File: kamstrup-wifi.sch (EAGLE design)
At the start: 25 parts, among them T1 BT137, T2 BT137, U1 ESP8266-07, U2 MCP1316T-29LE/OT

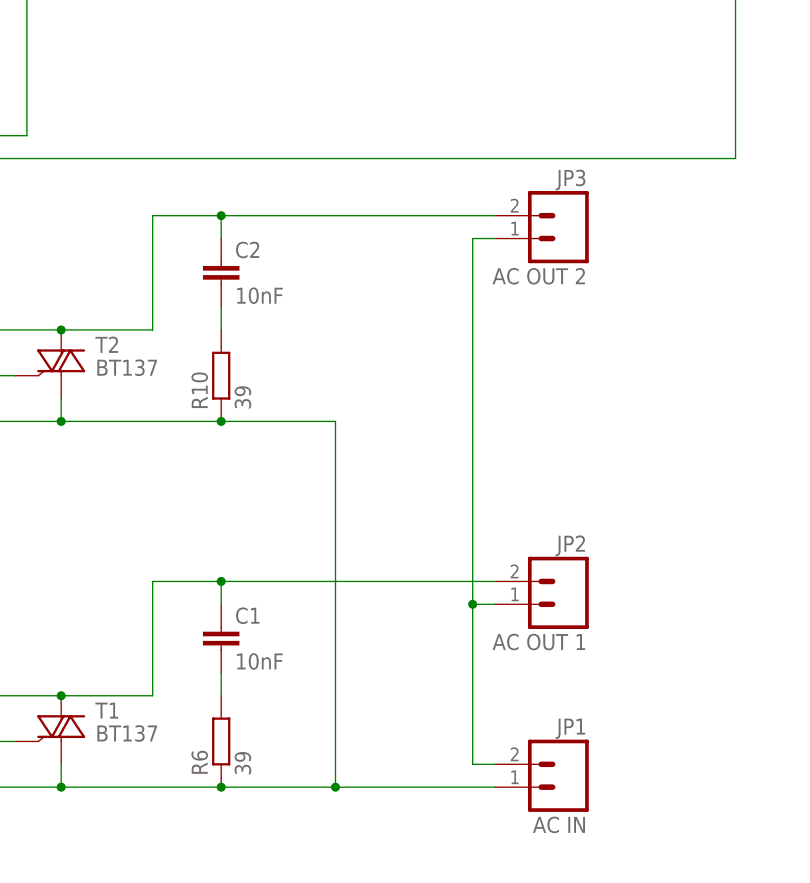
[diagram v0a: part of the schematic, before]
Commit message: rotated jp1, jp3 and jp3
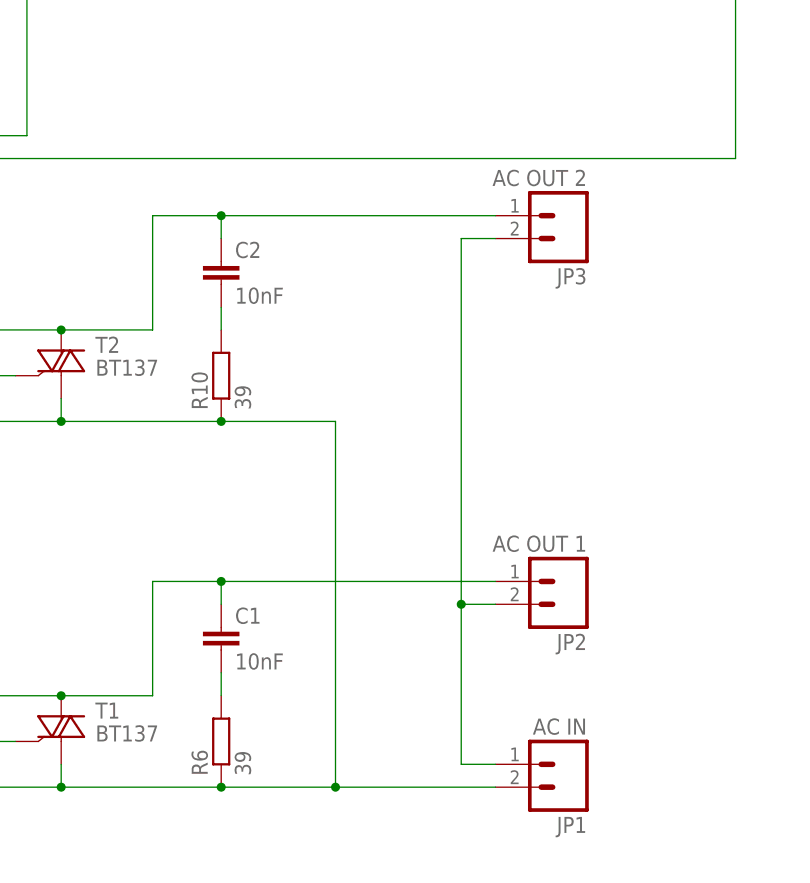
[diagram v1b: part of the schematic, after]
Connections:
- net N$15: now also JP2.1; no longer JP2.2
- net N$18: now also JP1.1, JP2.2, JP3.2; no longer JP1.2, JP2.1, JP3.1
- net N$8: now also JP3.1; no longer JP3.2
- net N$9: now also JP1.2; no longer JP1.1
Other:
- moved on the sheet: JP1, JP2, JP3
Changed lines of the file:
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@@
 <?xml version="1.0" encoding="utf-8"?>
 <!DOCTYPE eagle SYSTEM "eagle.dtd">
-<eagle version="8.2.1">
+<eagle version="8.4.0">
 <drawing>
 <settings>
 <setting alwaysvectorfont="yes"/>
+<setting keepoldvectorfont="yes"/>
 <setting verticaltext="up"/>
 </settings>
@@
 <instance part="R10" gate="G$1" x="97.79" y="-31.75" rot="R90"/>
 <instance part="C2" gate="G$1" x="97.79" y="-19.05"/>
-<instance part="JP3" gate="G$1" x="135.89" y="-16.51" rot="MR0"/>
+<instance part="JP3" gate="G$1" x="135.89" y="-13.97" rot="R180"/>
 <instance part="OK1" gate="-1" x="46.99" y="-72.39"/>
 <instance part="GND2" gate="1" x="31.75" y="-82.55"/>
@@
 <instance part="R6" gate="G$1" x="97.79" y="-72.39" rot="R90"/>
 <instance part="C1" gate="G$1" x="97.79" y="-59.69"/>
-<instance part="JP1" gate="G$1" x="135.89" y="-77.47" rot="MR0"/>
-<instance part="JP2" gate="G$1" x="135.89" y="-57.15" rot="MR0"/>
+<instance part="JP1" gate="G$1" x="135.89" y="-74.93" rot="R180"/>
+<instance part="JP2" gate="G$1" x="135.89" y="-54.61" rot="R180"/>
 <instance part="T1" gate="G$1" x="80.01" y="-72.39"/>
 <instance part="T2" gate="G$1" x="80.01" y="-31.75"/>
@@
 <pinref part="T2" gate="G$1" pin="A2"/>
 <junction x="80.01" y="-26.67"/>
-<pinref part="JP3" gate="G$1" pin="2"/>
+<pinref part="JP3" gate="G$1" pin="1"/>
 <wire x1="128.27" y1="-13.97" x2="97.79" y2="-13.97" width="0.1524" layer="91"/>
 <junction x="97.79" y="-13.97"/>
@@
 <wire x1="110.49" y1="-36.83" x2="110.49" y2="-77.47" width="0.1524" layer="91"/>
 <junction x="97.79" y="-36.83"/>
-<pinref part="JP1" gate="G$1" pin="1"/>
+<pinref part="T2" gate="G$1" pin="A1"/>
+<pinref part="T1" gate="G$1" pin="A1"/>
+<pinref part="JP1" gate="G$1" pin="2"/>
 <wire x1="110.49" y1="-77.47" x2="128.27" y2="-77.47" width="0.1524" layer="91"/>
 <junction x="110.49" y="-77.47"/>
-<pinref part="T2" gate="G$1" pin="A1"/>
-<pinref part="T1" gate="G$1" pin="A1"/>
 </segment>
 </net>
@@
 <pinref part="T1" gate="G$1" pin="A2"/>
 <junction x="80.01" y="-67.31"/>
-<pinref part="JP2" gate="G$1" pin="2"/>
-<wire x1="128.27" y1="-54.61" x2="97.79" y2="-54.61" width="0.1524" layer="91"/>
+<pinref part="JP2" gate="G$1" pin="1"/>
+<wire x1="97.79" y1="-54.61" x2="128.27" y2="-54.61" width="0.1524" layer="91"/>
 <junction x="97.79" y="-54.61"/>
 </segment>
@@
 <pinref part="C1" gate="G$1" pin="2"/>
 <wire x1="97.79" y1="-67.31" x2="97.79" y2="-64.77" width="0.1524" layer="91"/>
-</segment>
-</net>
-<net name="N$18" class="0">
-<segment>
-<wire x1="125.73" y1="-74.93" x2="125.73" y2="-57.15" width="0.1524" layer="91"/>
-<wire x1="125.73" y1="-57.15" x2="125.73" y2="-16.51" width="0.1524" layer="91"/>
-<pinref part="JP1" gate="G$1" pin="2"/>
-<wire x1="128.27" y1="-74.93" x2="125.73" y2="-74.93" width="0.1524" layer="91"/>
-<pinref part="JP2" gate="G$1" pin="1"/>
-<wire x1="128.27" y1="-57.15" x2="125.73" y2="-57.15" width="0.1524" layer="91"/>
-<junction x="125.73" y="-57.15"/>
-<pinref part="JP3" gate="G$1" pin="1"/>
-<wire x1="128.27" y1="-16.51" x2="125.73" y2="-16.51" width="0.1524" layer="91"/>
 </segment>
 </net>
@@
 </segment>
 </net>
+<net name="N$18" class="0">
+<segment>
+<pinref part="JP3" gate="G$1" pin="2"/>
+<wire x1="128.27" y1="-16.51" x2="124.46" y2="-16.51" width="0.1524" layer="91"/>
+<pinref part="JP1" gate="G$1" pin="1"/>
+<wire x1="124.46" y1="-16.51" x2="124.46" y2="-57.15" width="0.1524" layer="91"/>
+<wire x1="124.46" y1="-57.15" x2="124.46" y2="-74.93" width="0.1524" layer="91"/>
+<wire x1="124.46" y1="-74.93" x2="128.27" y2="-74.93" width="0.1524" layer="91"/>
+<pinref part="JP2" gate="G$1" pin="2"/>
+<wire x1="128.27" y1="-57.15" x2="124.46" y2="-57.15" width="0.1524" layer="91"/>
+<junction x="124.46" y="-57.15"/>
+</segment>
+</net>

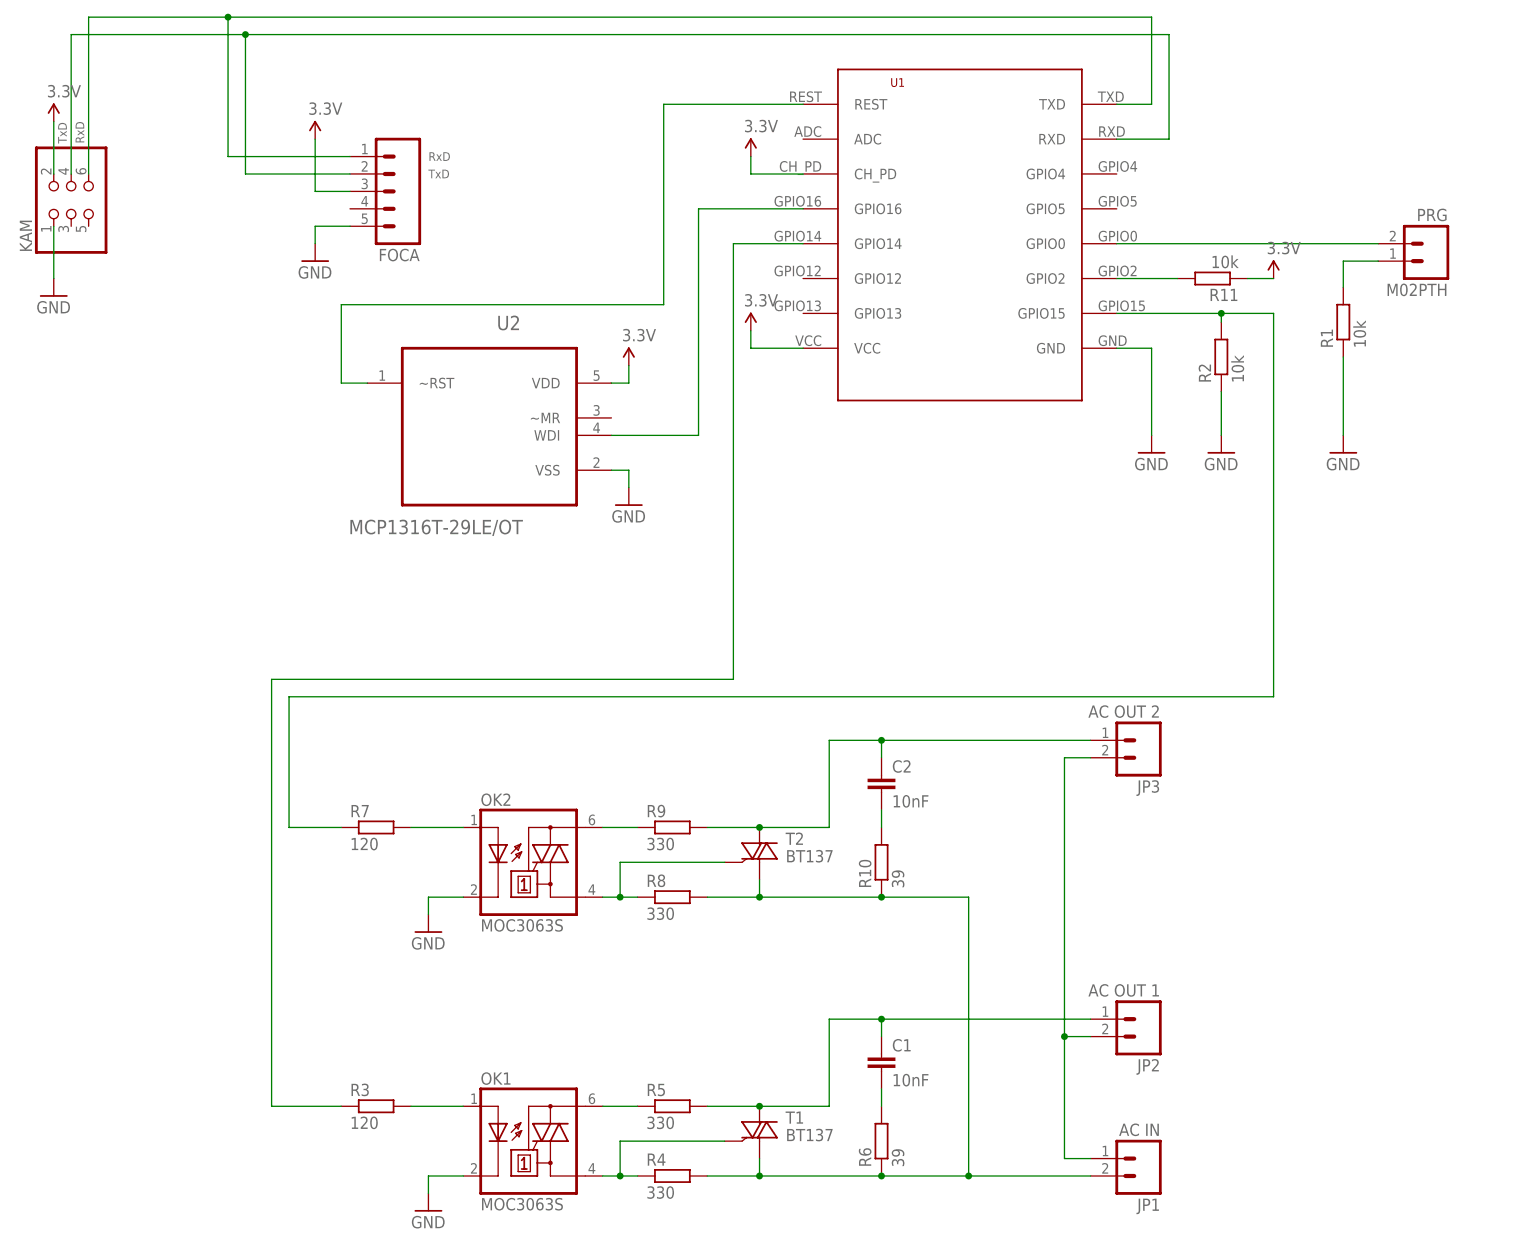
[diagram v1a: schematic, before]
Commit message: removed snubber circuits and external watchdog timer ic now version 1.3.0
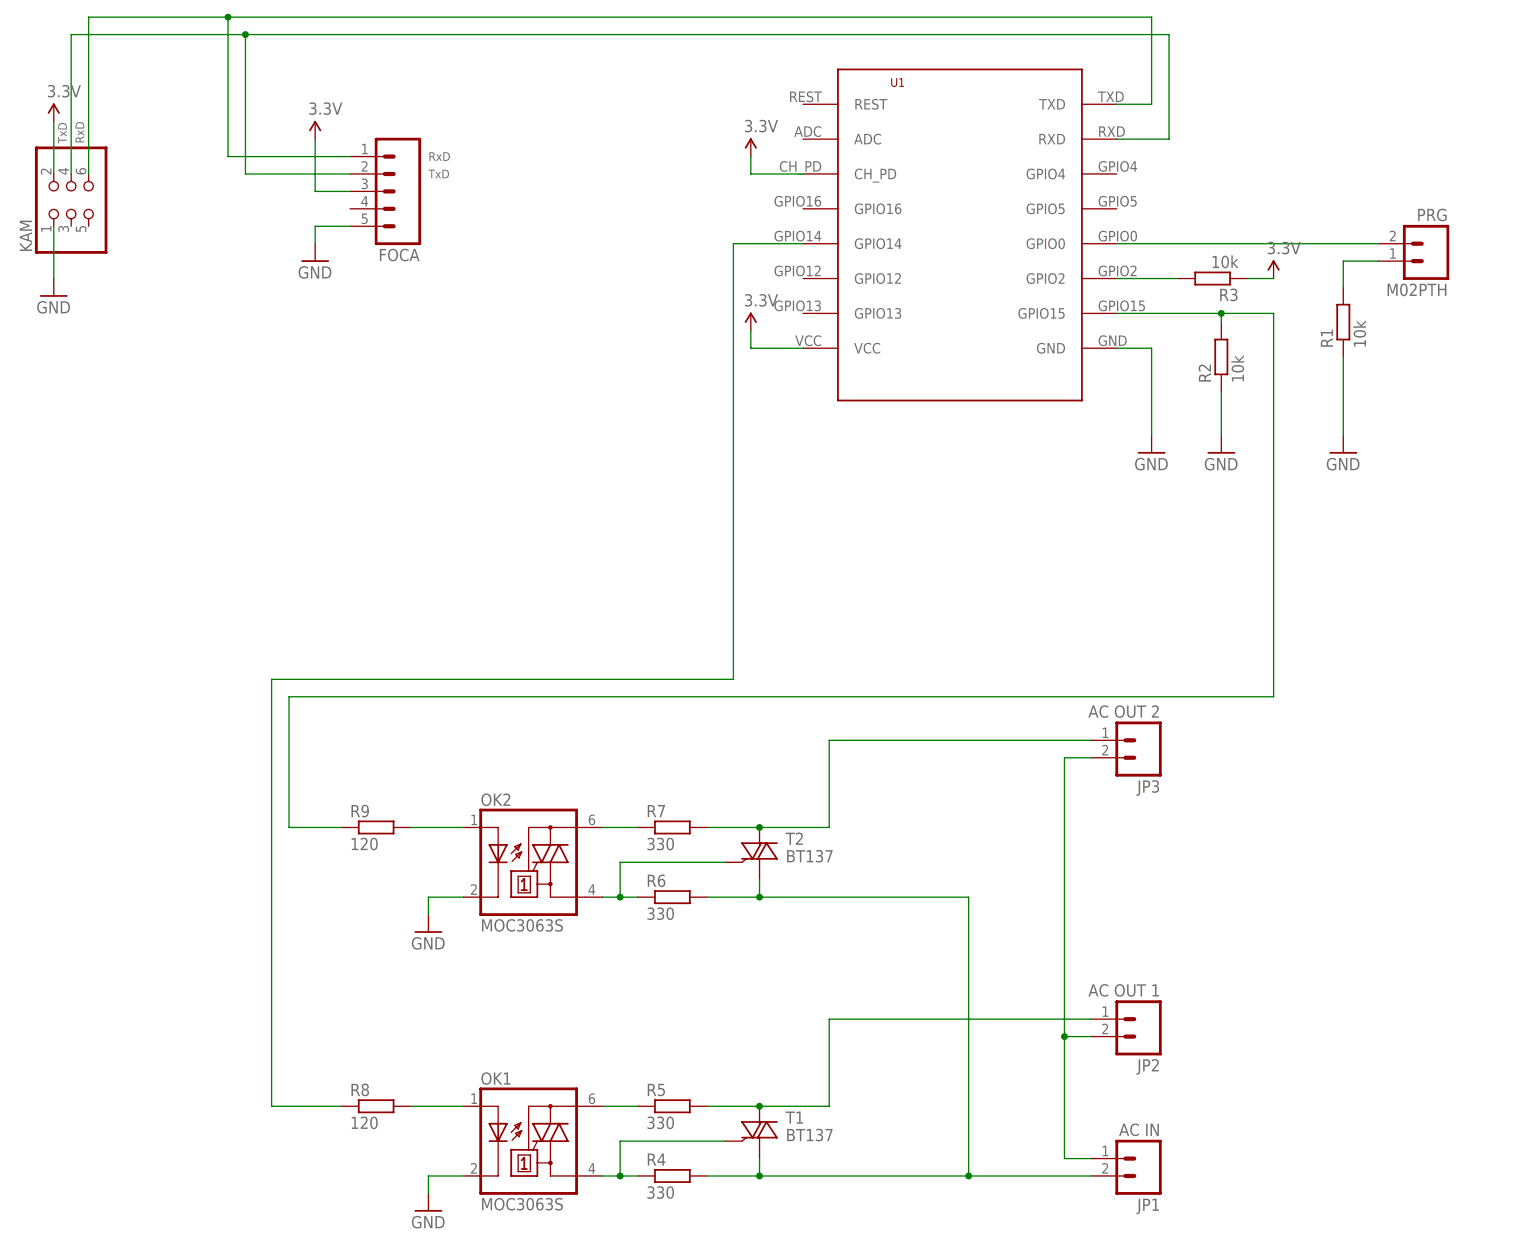
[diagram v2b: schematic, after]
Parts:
- removed C1, C2: 10nF, rcl:C-EUC1206
- removed R10: 39, rcl:R-EU_R0805
- removed R11: 10k, rcl:R-EU_R0805
- removed U2: MCP1316T-29LE/OT, Microchip_By_element14_Batch_1:MCP1316T-29LE/OT
- R3: value 120 -> 10k
- R6: value 39 -> 330
- R7: value 120 -> 330
- R8, R9: value 330 -> 120
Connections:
- removed net N$10: C2.2, R10.2
- removed net N$17: C1.2, R6.2
- removed net N$19: U1.REST, U2.~RST
- removed net N$20: U1.GPIO16, U2.WDI
- net 3.3V: now also R3.1; no longer R11.1, U2.VDD
- net GND: no longer U2.VSS
- net N$11: now also R8.1; no longer R3.1
- net N$12: now also R8.2; no longer R3.2
- net N$15: no longer C1.1
- net N$16: now also R9.1; no longer R7.1
- net N$21: now also R3.2; no longer R11.2
- net N$5: now also R9.2; no longer R7.2
- net N$6: now also R6.1; no longer R8.1
- net N$7: now also R7.1; no longer R9.1
- net N$8: now also R7.2; no longer C2.1, R9.2
- net N$9: now also R6.2; no longer R10.1, R6.1, R8.2
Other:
- moved on the sheet: R3, R6, R7, R8, R9

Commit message: Sdcard
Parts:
- added U$1: MICROSD_SPI_MODE, con-molex-microsd:MICROSD_SPI_MODE
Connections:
- new net N$10: U$1.DO, U1.GPIO12
- new net N$17: U$1.DI, U1.GPIO13
- new net N$19: U$1.CLK, U1.GPIO14
- new net N$20: R2.2, U$1./CS, U1.GPIO15
- net 3.3V: now also U$1.VDD
- net GND: now also U$1.VSS
- net N$11: now also U1.GPIO4; no longer U1.GPIO14
- net N$16: now also U1.GPIO5; no longer R2.2, U1.GPIO15
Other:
- moved on the sheet: R2
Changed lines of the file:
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@@
 <?xml version="1.0" encoding="utf-8"?>
 <!DOCTYPE eagle SYSTEM "eagle.dtd">
-<eagle version="8.4.0">
+<eagle version="9.0.1">
 <drawing>
 <settings>
-<setting alwaysvectorfont="yes"/>
+<setting alwaysvectorfont="no"/>
 <setting keepoldvectorfont="yes"/>
 <setting verticaltext="up"/>
 </settings>
-<grid distance="0.1" unitdist="inch" unit="inch" style="lines" multiple="1" display="no" altdistance="0.01" altunitdist="inch" altunit="inch"/>
+<grid distance="0.05" unitdist="inch" unit="inch" style="lines" multiple="1" display="no" altdistance="0.005" altunitdist="inch" altunit="inch"/>
 <layers>
 <layer number="1" name="Top" color="4" fill="1" visible="no" active="no"/>
@@
 <part name="SUPPLY5" library="SparkFun-Aesthetics" deviceset="3.3V" device=""/>
 <part name="R3" library="rcl" deviceset="R-EU_" device="R0805" value="10k"/>
+<part name="U$1" library="con-molex-microsd" deviceset="MICROSD_SPI_MODE" device=""/>
+<part name="GND7" library="SparkFun-Aesthetics" deviceset="GND" device=""/>
+<part name="SUPPLY3" library="SparkFun-Aesthetics" deviceset="3.3V" device=""/>
 </parts>
 <sheets>
@@
 <instance part="SUPPLY2" gate="G$1" x="78.74" y="71.12"/>
 <instance part="SUPPLY7" gate="G$1" x="78.74" y="45.72"/>
-<instance part="R2" gate="G$1" x="147.32" y="41.91" rot="R90"/>
-<instance part="GND3" gate="1" x="147.32" y="27.94"/>
+<instance part="R2" gate="G$1" x="151.13" y="48.26" rot="R180"/>
+<instance part="GND3" gate="1" x="157.48" y="27.94"/>
 <instance part="SUPPLY5" gate="G$1" x="154.94" y="53.34"/>
 <instance part="R3" gate="G$1" x="146.05" y="53.34" rot="R180"/>
+<instance part="U$1" gate="G$1" x="27.94" y="25.4" rot="MR180"/>
+<instance part="GND7" gate="1" x="48.26" y="22.86"/>
+<instance part="SUPPLY3" gate="G$1" x="58.42" y="20.32"/>
 </instances>
 <busses>
@@
 <pinref part="GND3" gate="1" pin="GND"/>
 <pinref part="R2" gate="G$1" pin="1"/>
-<wire x1="147.32" y1="30.48" x2="147.32" y2="36.83" width="0.1524" layer="91"/>
+<wire x1="157.48" y1="30.48" x2="157.48" y2="45.72" width="0.1524" layer="91"/>
+<wire x1="157.48" y1="45.72" x2="157.48" y2="48.26" width="0.1524" layer="91"/>
+<wire x1="157.48" y1="48.26" x2="156.21" y2="48.26" width="0.1524" layer="91"/>
+</segment>
+<segment>
+<pinref part="U$1" gate="G$1" pin="VSS"/>
+<pinref part="GND7" gate="1" pin="GND"/>
+<wire x1="40.64" y1="25.4" x2="48.26" y2="25.4" width="0.1524" layer="91"/>
 </segment>
 </net>
@@
 <pinref part="SUPPLY5" gate="G$1" pin="3.3V"/>
 <wire x1="151.13" y1="53.34" x2="154.94" y2="53.34" width="0.1524" layer="91"/>
+</segment>
+<segment>
+<pinref part="U$1" gate="G$1" pin="VDD"/>
+<pinref part="SUPPLY3" gate="G$1" pin="3.3V"/>
+<wire x1="40.64" y1="20.32" x2="58.42" y2="20.32" width="0.1524" layer="91"/>
 </segment>
 </net>
@@
 <net name="N$11" class="0">
 <segment>
-<wire x1="76.2" y1="-5.08" x2="76.2" y2="58.42" width="0.1524" layer="91"/>
-<pinref part="U1" gate="G$1" pin="GPIO14"/>
-<wire x1="76.2" y1="58.42" x2="86.36" y2="58.42" width="0.1524" layer="91"/>
-<wire x1="76.2" y1="-5.08" x2="8.89" y2="-5.08" width="0.1524" layer="91"/>
 <wire x1="8.89" y1="-5.08" x2="8.89" y2="-67.31" width="0.1524" layer="91"/>
 <pinref part="R8" gate="G$1" pin="1"/>
 <wire x1="8.89" y1="-67.31" x2="19.05" y2="-67.31" width="0.1524" layer="91"/>
+<wire x1="8.89" y1="-5.08" x2="189.23" y2="-5.08" width="0.1524" layer="91"/>
+<pinref part="U1" gate="G$1" pin="GPIO4"/>
+<wire x1="189.23" y1="-5.08" x2="189.23" y2="68.58" width="0.1524" layer="91"/>
+<wire x1="189.23" y1="68.58" x2="132.08" y2="68.58" width="0.1524" layer="91"/>
 </segment>
 </net>
 <net name="N$16" class="0">
 <segment>
-<wire x1="154.94" y1="-7.62" x2="154.94" y2="48.26" width="0.1524" layer="91"/>
-<pinref part="U1" gate="G$1" pin="GPIO15"/>
-<wire x1="154.94" y1="48.26" x2="147.32" y2="48.26" width="0.1524" layer="91"/>
-<pinref part="R2" gate="G$1" pin="2"/>
-<wire x1="147.32" y1="48.26" x2="132.08" y2="48.26" width="0.1524" layer="91"/>
-<wire x1="147.32" y1="46.99" x2="147.32" y2="48.26" width="0.1524" layer="91"/>
-<junction x="147.32" y="48.26"/>
 <pinref part="R9" gate="G$1" pin="1"/>
 <wire x1="11.43" y1="-26.67" x2="19.05" y2="-26.67" width="0.1524" layer="91"/>
-<wire x1="154.94" y1="-7.62" x2="11.43" y2="-7.62" width="0.1524" layer="91"/>
 <wire x1="11.43" y1="-7.62" x2="11.43" y2="-26.67" width="0.1524" layer="91"/>
+<wire x1="11.43" y1="-7.62" x2="191.77" y2="-7.62" width="0.1524" layer="91"/>
+<pinref part="U1" gate="G$1" pin="GPIO5"/>
+<wire x1="191.77" y1="-7.62" x2="191.77" y2="63.5" width="0.1524" layer="91"/>
+<wire x1="191.77" y1="63.5" x2="132.08" y2="63.5" width="0.1524" layer="91"/>
 </segment>
 </net>
@@
 </segment>
 </net>
+<net name="N$10" class="0">
+<segment>
+<pinref part="U1" gate="G$1" pin="GPIO12"/>
+<wire x1="86.36" y1="53.34" x2="48.26" y2="53.34" width="0.1524" layer="91"/>
+<wire x1="48.26" y1="53.34" x2="48.26" y2="27.94" width="0.1524" layer="91"/>
+<pinref part="U$1" gate="G$1" pin="DO"/>
+<wire x1="48.26" y1="27.94" x2="40.64" y2="27.94" width="0.1524" layer="91"/>
+</segment>
+</net>
+<net name="N$17" class="0">
+<segment>
+<pinref part="U$1" gate="G$1" pin="DI"/>
+<wire x1="40.64" y1="17.78" x2="53.34" y2="17.78" width="0.1524" layer="91"/>
+<wire x1="53.34" y1="17.78" x2="53.34" y2="48.26" width="0.1524" layer="91"/>
+<pinref part="U1" gate="G$1" pin="GPIO13"/>
+<wire x1="53.34" y1="48.26" x2="86.36" y2="48.26" width="0.1524" layer="91"/>
+</segment>
+</net>
+<net name="N$19" class="0">
+<segment>
+<pinref part="U1" gate="G$1" pin="GPIO14"/>
+<wire x1="86.36" y1="58.42" x2="43.18" y2="58.42" width="0.1524" layer="91"/>
+<wire x1="43.18" y1="58.42" x2="43.18" y2="22.86" width="0.1524" layer="91"/>
+<pinref part="U$1" gate="G$1" pin="CLK"/>
+<wire x1="43.18" y1="22.86" x2="40.64" y2="22.86" width="0.1524" layer="91"/>
+</segment>
+</net>
+<net name="N$20" class="0">
+<segment>
+<pinref part="U1" gate="G$1" pin="GPIO15"/>
+<pinref part="R2" gate="G$1" pin="2"/>
+<wire x1="146.05" y1="48.26" x2="144.78" y2="48.26" width="0.1524" layer="91"/>
+<pinref part="U$1" gate="G$1" pin="/CS"/>
+<wire x1="144.78" y1="48.26" x2="132.08" y2="48.26" width="0.1524" layer="91"/>
+<wire x1="40.64" y1="15.24" x2="144.78" y2="15.24" width="0.1524" layer="91"/>
+<wire x1="144.78" y1="15.24" x2="144.78" y2="48.26" width="0.1524" layer="91"/>
+<junction x="144.78" y="48.26"/>
+</segment>
+</net>
